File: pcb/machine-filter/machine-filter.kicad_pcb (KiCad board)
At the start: 4 copper layers, 150 x 107 mm, 0 parts

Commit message: Placement step 1: footprints in the PCB, grouped by function; zone sketch
- Footprints brought into the PCB through Konnect (KiCad 10 IPC) and sorted into
  function groups beside their boards (design/groups.py, stage_groups.py,
  tools/konnect_stage.py), plus 8 optional standoff holes and group labels.
- Main-board zone sketch with area budgets for review (design/zone_sketch.py,
  out/zone-sketch.png).
- WIDTH moved to U1 so each CV quad carries one 1V/OCT channel (d).
- gen_sch.py: stable sheet/symbol UUIDs, so rebuilds keep PCB links.
- Both boards 2-layer (d); Konnect setup notes; CLAUDE.md: pin map follows
  the layout.

Co-Authored-By: Claude Opus 5.5 <noreply@anthropic.com>
Claude-Session: https://claude.ai/code/session_01Cf5qNBi3oNHhbCjPHvswth
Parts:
- added A1: Daisy Seed3, filter-module:Daisy_Seed_ES_Sockets, F.Cu at (263.9, 69.5)
- added C1: 10u 25V, filter-module:C_0805, F.Cu at (328.6, 119.7)
- added C10: 1n, filter-module:C_0603, F.Cu at (292.0, 138.7)
- added C100: 100n, filter-module:C_0603, F.Cu at (324.8, 168.2)
- added C11: 1n, filter-module:C_0603, F.Cu at (292.0, 164.2)
- added C12: 1n, filter-module:C_0603, F.Cu at (278.3, 149.6)
- added C13: 1n, filter-module:C_0603, F.Cu at (264.0, 152.6)
- added C14: 1n, filter-module:C_0603, F.Cu at (283.0, 152.6)
- added C15: 1n, filter-module:C_0603, F.Cu at (278.3, 175.1)
- added C16: 1n, filter-module:C_0603, F.Cu at (264.0, 178.1)
- added C17: 1n, filter-module:C_0603, F.Cu at (283.0, 178.1)
- added C2: 100u 35V, Capacitor_SMD:CP_Elec_6.3x7.7, F.Cu at (309.1, 145.2)
- added C20: 100n, filter-module:C_0603, F.Cu at (273.0, 164.2)
- added C21: 100n, filter-module:C_0603, F.Cu at (273.0, 138.7)
- added C3: 10u 25V, filter-module:C_0805, F.Cu at (328.1, 142.6)
- added C4: 100u 35V, Capacitor_SMD:CP_Elec_6.3x7.7, F.Cu at (309.1, 153.9)
- added C5: 100u 35V, Capacitor_SMD:CP_Elec_6.3x7.7, F.Cu at (273.2, 124.4)
- added C50: 330p, filter-module:C_0603, F.Cu at (334.1, 68.8)
- added C52: 330p, filter-module:C_0603, F.Cu at (320.3, 75.8)
- added C6: 100u 35V, Capacitor_SMD:CP_Elec_6.3x7.7, F.Cu at (291.7, 71.6)
- added C60: 47p, filter-module:C_0603, F.Cu at (334.1, 87.4)
- added C62: 47p, filter-module:C_0603, F.Cu at (320.3, 94.4)
- added C7: 100n, filter-module:C_0603, F.Cu at (311.0, 106.0)
- added C70: 100n, filter-module:C_0603, F.Cu at (315.1, 68.8)
- added C71: 100n, filter-module:C_0603, F.Cu at (319.8, 68.8)
- added C72: 100n, filter-module:C_0603, F.Cu at (315.1, 87.4)
- added C73: 100n, filter-module:C_0603, F.Cu at (319.8, 87.4)
- added C80: 100n, Capacitor_THT:C_Disc_D3.0mm_W1.6mm_P2.50mm, F.Cu at (84.8, 65.8)
- added C81: 100n, Capacitor_THT:C_Disc_D3.0mm_W1.6mm_P2.50mm, F.Cu at (65.8, 86.4)
- added C82: 100n, Capacitor_THT:C_Disc_D3.0mm_W1.6mm_P2.50mm, F.Cu at (72.0, 86.4)
- added C83: 100n, Capacitor_THT:C_Disc_D3.0mm_W1.6mm_P2.50mm, F.Cu at (65.8, 116.7)
- added C84: 100n, Capacitor_THT:C_Disc_D3.0mm_W1.6mm_P2.50mm, F.Cu at (72.0, 116.7)
- added D1: red 3 mm, filter-module:LED_3mm_C1A2, F.Cu at (2.94, 93.3)
- added D10: B5819W, filter-module:D_SOD-123, F.Cu at (323.1, 119.6)
- added D11: B5819W, filter-module:D_SOD-123, F.Cu at (322.6, 142.5)
- added D2: red/green 3 mm, filter-module:LED_3mm_Raised, F.Cu at (8.99, 92.1)
- added D3: red/green 3 mm, filter-module:LED_3mm_Raised, F.Cu at (14.8, 92.1)
- added D4: red/green 3 mm, filter-module:LED_3mm_Raised, F.Cu at (20.7, 92.1)
- added D5: red/green 3 mm, filter-module:LED_3mm_Raised, F.Cu at (-42.0, 103.0)
- added D6: red/green 3 mm, filter-module:LED_3mm_Raised, F.Cu at (-36.2, 103.0)
- added D7: red/green 3 mm, filter-module:LED_3mm_Raised, F.Cu at (-30.3, 103.0)
- added D8: red/green 3 mm, filter-module:LED_3mm_Raised, F.Cu at (-24.5, 103.0)
- added D9: red/green 3 mm, filter-module:LED_3mm_Raised, F.Cu at (-18.6, 103.0)
- added FB1: 600R@100MHz 0.5A, filter-module:R_0805_2012Metric, F.Cu at (317.5, 119.7)
- added FB2: 600R@100MHz 0.5A, filter-module:R_0805_2012Metric, F.Cu at (317.0, 142.6)
- added H1: MountingHole_3.2mm_M3, MountingHole:MountingHole_3.2mm_M3, F.Cu at (266.4, 194.8)
- added H11: MountingHole_3.2mm_M3, MountingHole:MountingHole_3.2mm_M3, F.Cu at (-40.2, 156.8)
- added H12: MountingHole_3.2mm_M3, MountingHole:MountingHole_3.2mm_M3, F.Cu at (-32.2, 156.8)
- added H13: MountingHole_3.2mm_M3, MountingHole:MountingHole_3.2mm_M3, F.Cu at (-24.2, 156.8)
- added H14: MountingHole_3.2mm_M3, MountingHole:MountingHole_3.2mm_M3, F.Cu at (-16.2, 156.8)
- added H2: MountingHole_3.2mm_M3, MountingHole:MountingHole_3.2mm_M3, F.Cu at (274.4, 194.8)
- added H3: MountingHole_3.2mm_M3, MountingHole:MountingHole_3.2mm_M3, F.Cu at (282.4, 194.8)
- added H4: MountingHole_3.2mm_M3, MountingHole:MountingHole_3.2mm_M3, F.Cu at (290.4, 194.8)
- added J1: PJ398SM, filter-module:PJ398SM_Jack_ES, F.Cu at (-39.4, 71.0)
- added J10: PJ398SM, filter-module:PJ398SM_Jack_4ms_BentGND, F.Cu at (-37.7, 95.7)
- added J11: PJ398SM, filter-module:PJ398SM_Jack_4ms_BentGND, F.Cu at (-22.8, 95.7)
- added J12: PJ398SM, filter-module:PJ398SM_Jack_4ms_BentGND, F.Cu at (-7.89, 95.7)
- added J13: EURO PWR 2x5, filter-module:Pins_2x05_2.54mm_TH_EurorackPower_Shrouded, F.Cu at (309.4, 129.5)
- added J14: EXPANSION 2x4, filter-module:Pins_2x04_2.54mm_TH, F.Cu at (346.6, 73.2)
- added J15: TF-01A, filter-module:TF-01A, F.Cu at (313.1, 175.3)
- added J2: PJ398SM, filter-module:PJ398SM_Jack_ES, F.Cu at (-28.4, 71.0)
- added J3: PJ398SM, filter-module:PJ398SM_Jack_ES, F.Cu at (-17.3, 71.0)
- added J4: PJ398SM, filter-module:PJ398SM_Jack_ES, F.Cu at (-6.26, 71.0)
- added J5: PJ398SM, filter-module:PJ398SM_Jack_4ms_BentGND, F.Cu at (6.47, 69.5)
- added J6: PJ398SM, filter-module:PJ398SM_Jack_4ms_BentGND, F.Cu at (-37.7, 84.7)
- added J7: PJ398SM, filter-module:PJ398SM_Jack_4ms_BentGND, F.Cu at (-22.8, 84.7)
- added J8: PJ398SM, filter-module:PJ398SM_Jack_4ms_BentGND, F.Cu at (-7.89, 84.7)
- added J9: PJ398SM, filter-module:PJ398SM_Jack_4ms_BentGND, F.Cu at (7.03, 84.7)
- added JA1: 1x15 socket, Connector_PinSocket_2.54mm:PinSocket_1x15_P2.54mm_Vertical, F.Cu at (35.8, 66.5)
- added JA2: 1x13 socket, Connector_PinSocket_2.54mm:PinSocket_1x13_P2.54mm_Vertical, F.Cu at (40.9, 66.5)
- added JA3: 1x10 socket, Connector_PinSocket_2.54mm:PinSocket_1x10_P2.54mm_Vertical, F.Cu at (46.0, 66.5)
- added JB1: 1x15 header, Connector_PinHeader_2.54mm:PinHeader_1x15_P2.54mm_Vertical, F.Cu at (345.7, 90.1)
- added JB2: 1x13 header, Connector_PinHeader_2.54mm:PinHeader_1x13_P2.54mm_Vertical, F.Cu at (350.8, 90.1)
- added JB3: 1x10 header, Connector_PinHeader_2.54mm:PinHeader_1x10_P2.54mm_Vertical, F.Cu at (355.9, 90.1)
- added R1: 3.3 0.75W, filter-module:R_1206_3216Metric, F.Cu at (281.8, 122.0)
- added R10: 100k 0.1%, filter-module:R_0603, F.Cu at (277.7, 138.7)
- added R100: 47k, filter-module:R_0603, F.Cu at (329.5, 168.2)
- added R101: 47k, filter-module:R_0603, F.Cu at (334.3, 168.2)
- added R102: 47k, filter-module:R_0603, F.Cu at (306.0, 182.1)
- added R103: 47k, filter-module:R_0603, F.Cu at (310.8, 182.1)
- added R104: 47k, filter-module:R_0603, F.Cu at (315.5, 182.1)
- added R11: 20k 0.1%, filter-module:R_0603, F.Cu at (287.2, 138.7)
- added R12: 120k 25ppm, filter-module:R_0603, F.Cu at (264.0, 149.6)
- added R13: 20k 0.1%, filter-module:R_0603, F.Cu at (282.5, 138.7)
- added R14: 100k 0.1%, filter-module:R_0603, F.Cu at (277.7, 164.2)
- added R15: 20k 0.1%, filter-module:R_0603, F.Cu at (287.2, 164.2)
- added R16: 120k 25ppm, filter-module:R_0603, F.Cu at (264.0, 175.1)
- added R17: 20k 0.1%, filter-module:R_0603, F.Cu at (282.5, 164.2)
- added R18: 120k, filter-module:R_0603, F.Cu at (268.8, 149.6)
- added R19: 20k, filter-module:R_0603, F.Cu at (273.5, 149.6)
- added R2: 3.3 0.75W, filter-module:R_1206_3216Metric, F.Cu at (264.7, 122.0)
- added R20: 120k, filter-module:R_0603, F.Cu at (283.0, 149.6)
- added R22: 120k, filter-module:R_0603, F.Cu at (287.8, 149.6)
- added R23: 20k, filter-module:R_0603, F.Cu at (292.5, 149.6)
- added R24: 120k, filter-module:R_0603, F.Cu at (268.8, 152.6)
- added R26: 120k, filter-module:R_0603, F.Cu at (273.5, 152.6)
- added R27: 20k, filter-module:R_0603, F.Cu at (278.3, 152.6)
- added R28: 120k, filter-module:R_0603, F.Cu at (287.8, 152.6)
- added R3: 1k, filter-module:R_0603, F.Cu at (315.7, 106.0)
- added R30: 120k, filter-module:R_0603, F.Cu at (268.8, 175.1)
- added R31: 20k, filter-module:R_0603, F.Cu at (273.5, 175.1)
- added R32: 120k, filter-module:R_0603, F.Cu at (283.0, 175.1)
- added R34: 120k, filter-module:R_0603, F.Cu at (287.8, 175.1)
- added R35: 20k, filter-module:R_0603, F.Cu at (292.5, 175.1)
- added R36: 120k, filter-module:R_0603, F.Cu at (268.8, 178.1)
- added R38: 120k, filter-module:R_0603, F.Cu at (273.5, 178.1)
- added R39: 20k, filter-module:R_0603, F.Cu at (278.3, 178.1)
- added R40: 120k, filter-module:R_0603, F.Cu at (287.8, 178.1)
- added R50: 100k, filter-module:R_0603, F.Cu at (324.6, 68.8)
- added R51: 10k, filter-module:R_0603, F.Cu at (329.3, 68.8)
- added R52: 100, filter-module:R_0603, F.Cu at (306.0, 75.8)
- added R54: 100k, filter-module:R_0603, F.Cu at (310.8, 75.8)
- added R55: 10k, filter-module:R_0603, F.Cu at (315.5, 75.8)
- added R56: 100, filter-module:R_0603, F.Cu at (325.0, 75.8)
- added R60: 10k, filter-module:R_0603, F.Cu at (324.6, 87.4)
- added R61: 51k, filter-module:R_0603, F.Cu at (329.3, 87.4)
- added R62: 100, filter-module:R_0603, F.Cu at (306.0, 94.4)
- added R64: 10k, filter-module:R_0603, F.Cu at (310.8, 94.4)
- added R65: 51k, filter-module:R_0603, F.Cu at (315.5, 94.4)
- added R66: 100, filter-module:R_0603, F.Cu at (325.0, 94.4)
- added R70: 1k, filter-module:R_0603, F.Cu at (283.8, 68.8)
- added R71: 1.5k, Resistor_THT:R_Axial_DIN0204_L3.6mm_D1.6mm_P5.08mm_Horizontal, F.Cu at (78.0, 86.4)
- added R72: 1.5k, Resistor_THT:R_Axial_DIN0204_L3.6mm_D1.6mm_P5.08mm_Horizontal, F.Cu at (56.8, 97.2)
- added R73: 1.5k, Resistor_THT:R_Axial_DIN0204_L3.6mm_D1.6mm_P5.08mm_Horizontal, F.Cu at (65.3, 97.2)
- added R74: 1.5k, Resistor_THT:R_Axial_DIN0204_L3.6mm_D1.6mm_P5.08mm_Horizontal, F.Cu at (73.8, 97.2)
- added R75: 1.5k, Resistor_THT:R_Axial_DIN0204_L3.6mm_D1.6mm_P5.08mm_Horizontal, F.Cu at (78.0, 116.7)
- added R76: 1.5k, Resistor_THT:R_Axial_DIN0204_L3.6mm_D1.6mm_P5.08mm_Horizontal, F.Cu at (56.8, 127.5)
- added R77: 1.5k, Resistor_THT:R_Axial_DIN0204_L3.6mm_D1.6mm_P5.08mm_Horizontal, F.Cu at (65.3, 127.5)
- added R78: 1.5k, Resistor_THT:R_Axial_DIN0204_L3.6mm_D1.6mm_P5.08mm_Horizontal, F.Cu at (73.8, 127.5)
- added R80: 10k, Resistor_THT:R_Axial_DIN0204_L3.6mm_D1.6mm_P5.08mm_Horizontal, F.Cu at (82.3, 97.2)
- added R81: 10k, Resistor_THT:R_Axial_DIN0204_L3.6mm_D1.6mm_P5.08mm_Horizontal, F.Cu at (56.8, 100.9)
- added R82: 10k, Resistor_THT:R_Axial_DIN0204_L3.6mm_D1.6mm_P5.08mm_Horizontal, F.Cu at (65.3, 100.9)
- added R83: 10k, Resistor_THT:R_Axial_DIN0204_L3.6mm_D1.6mm_P5.08mm_Horizontal, F.Cu at (73.8, 100.9)
- added R84: 10k, Resistor_THT:R_Axial_DIN0204_L3.6mm_D1.6mm_P5.08mm_Horizontal, F.Cu at (82.3, 127.5)
- added R85: 10k, Resistor_THT:R_Axial_DIN0204_L3.6mm_D1.6mm_P5.08mm_Horizontal, F.Cu at (56.8, 131.2)
- added R86: 10k, Resistor_THT:R_Axial_DIN0204_L3.6mm_D1.6mm_P5.08mm_Horizontal, F.Cu at (65.3, 131.2)
- added R87: 10k, Resistor_THT:R_Axial_DIN0204_L3.6mm_D1.6mm_P5.08mm_Horizontal, F.Cu at (73.8, 131.2)
- added R90: 1M, Resistor_THT:R_Axial_DIN0204_L3.6mm_D1.6mm_P5.08mm_Horizontal, F.Cu at (82.3, 100.9)
- added R91: 1M, Resistor_THT:R_Axial_DIN0204_L3.6mm_D1.6mm_P5.08mm_Horizontal, F.Cu at (56.8, 104.5)
- added R92: 1M, Resistor_THT:R_Axial_DIN0204_L3.6mm_D1.6mm_P5.08mm_Horizontal, F.Cu at (65.3, 104.5)
- added R93: 1M, Resistor_THT:R_Axial_DIN0204_L3.6mm_D1.6mm_P5.08mm_Horizontal, F.Cu at (73.8, 104.5)
- added R94: 1M, Resistor_THT:R_Axial_DIN0204_L3.6mm_D1.6mm_P5.08mm_Horizontal, F.Cu at (82.3, 131.2)
- added R95: 1M, Resistor_THT:R_Axial_DIN0204_L3.6mm_D1.6mm_P5.08mm_Horizontal, F.Cu at (56.8, 134.8)
- added R96: 1M, Resistor_THT:R_Axial_DIN0204_L3.6mm_D1.6mm_P5.08mm_Horizontal, F.Cu at (65.3, 134.8)
- added R97: 1M, Resistor_THT:R_Axial_DIN0204_L3.6mm_D1.6mm_P5.08mm_Horizontal, F.Cu at (73.8, 134.8)
- added RV1: B10k, filter-module:Pot_9mm_SnapIn_ES, F.Cu at (-8.62, 107.1)
- added RV2: B10k, filter-module:Pot_9mm_SnapIn_ES, F.Cu at (5.54, 107.1)
- added RV3: B10k, filter-module:Pot_9mm_SnapIn_ES, F.Cu at (19.7, 107.1)
- added RV4: B10k, filter-module:Pot_9mm_SnapIn_ES, F.Cu at (-37.9, 121.9)
- added RV5: B10k, filter-module:Pot_9mm_SnapIn_ES, F.Cu at (-23.7, 121.9)
- added RV6: B10k, filter-module:Pot_9mm_SnapIn_ES, F.Cu at (-9.56, 121.9)
- added RV7: B10k, filter-module:Pot_9mm_SnapIn_ES, F.Cu at (4.58, 121.9)
- added RV8: B10k, filter-module:Pot_9mm_SnapIn_ES, F.Cu at (18.7, 121.9)
- added RV9: B10k, filter-module:Pot_9mm_SnapIn_ES, F.Cu at (-37.9, 136.7)
- added U1: LMV324, filter-module:SOIC-14_3.9x8.65mm_Pitch1.27mm, F.Cu at (266.1, 168.1)
- added U2: LMV324, filter-module:SOIC-14_3.9x8.65mm_Pitch1.27mm, F.Cu at (266.1, 142.6)
- added U3: TL072, filter-module:SOIC-8_3.9x4.9mm_Pitch1.27mm, F.Cu at (308.2, 70.8)
- added U4: TL072, filter-module:SOIC-8_3.9x4.9mm_Pitch1.27mm, F.Cu at (308.2, 89.4)
- added U5: LM4040-10, filter-module:SOT-23, F.Cu at (306.1, 107.0)
- added U6: 74HC4051, filter-module:SOIC-16_3.9x9.9mm_Pitch1.27mm, F.Cu at (78.5, 70.0)
- added U7: LM324, filter-module:SOIC-14_3.9x8.65mm_Pitch1.27mm, F.Cu at (59.5, 90.0)
- added U8: LM324, filter-module:SOIC-14_3.9x8.65mm_Pitch1.27mm, F.Cu at (59.5, 120.3)
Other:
- board text added: "1 SEED3 (+ supply filter)"
- board text added: "2 CV U1: WIDTH (1V/OCT), EQ GAIN, DIST, SMPL RATE"
- board text added: "2 CV U2: BASE (1V/OCT), HP RES, LP RES, EQ FREQ"
- board text added: "3 AUDIO IN U3"
- board text added: "3 AUDIO OUT U4"
- board text added: "4 -10V REF U5"
- board text added: "5 POWER ENTRY J13"
- board text added: "6 EXPANSION J14"
- board text added: "6 microSD J15 (optional)"
- board text added: "7 HEADERS"
- board text added: "8 STANDOFFS (optional)"
- board text added: "LED DRIVERS U7"
- board text added: "LED DRIVERS U8"
- board text added: "PANEL PARTS (fixed by the panel)"
- board text added: "POT MUX U6"

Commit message: Placement step 2: Seed3 placed with its group; VIN trace; board set to 2 layers
- A1 on the main board's back at its USB-rule spot (pins checked against the
  zone sketch), supply filter R1-C5-R2-C6 at VIN, R70 at pin 12, and the first
  trace: Seed3 pin 39 -> C6 (0.5 mm, B.Cu).
- design/placement.py records each step; tools/konnect_place.py applies it
  through Konnect, checks pad positions before routing, and saves.
- Copper layers 4 -> 2 (d), set in KiCad's Board Setup.

Co-Authored-By: Claude Opus 5.5 <noreply@anthropic.com>
Claude-Session: https://claude.ai/code/session_01Cf5qNBi3oNHhbCjPHvswth
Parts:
- A1, C5, C6, R1, R2, R70: moved to B.Cu
- moved C6 88.1 mm to (237.5, 141.0)
- moved R70 86.6 mm to (208.5, 111.5), turned to 90 degrees
- moved A1 86.2 mm to (213.6, 139.5)
- moved R1 52.2 mm to (244.5, 158.5)
- moved C5 45.5 mm to (237.5, 152.5)
- moved R2 37.0 mm to (237.5, 147.0)
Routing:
- net VIN: track 0.00 -> 10.00 mm
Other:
- copper layers 4 -> 2

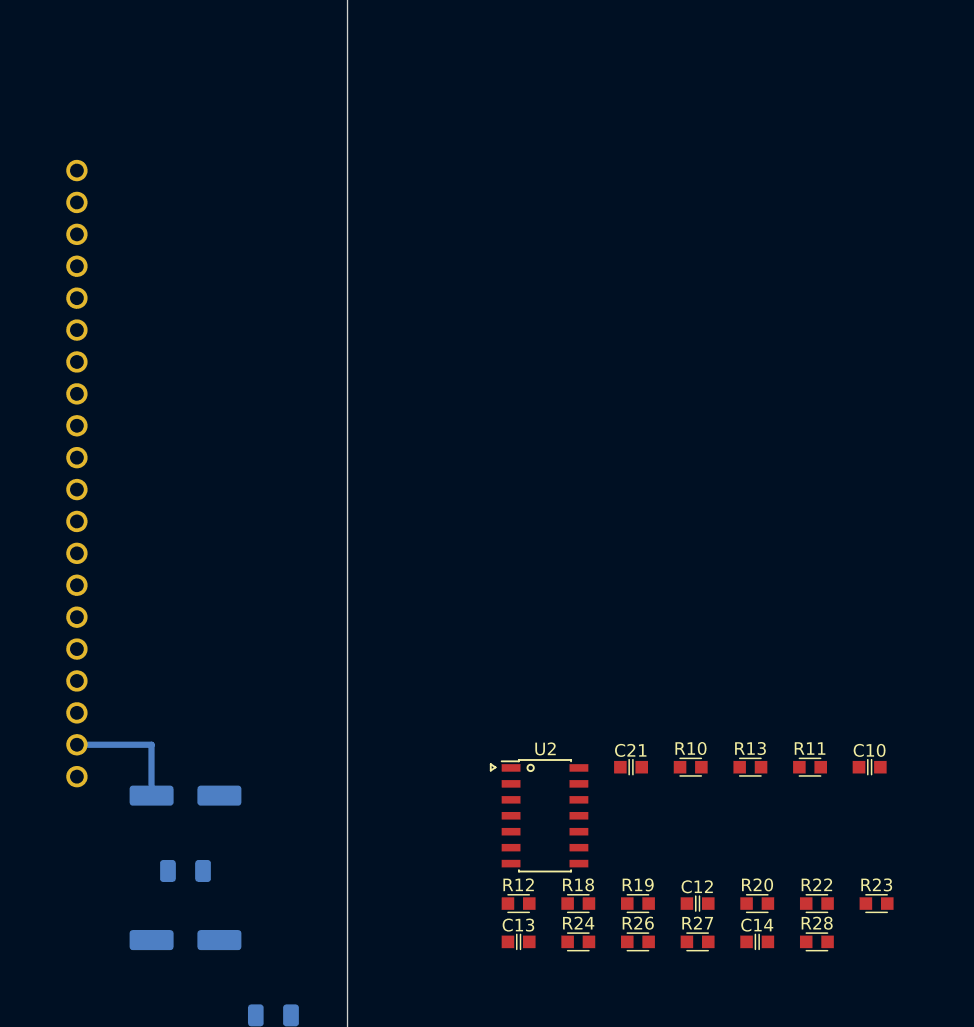
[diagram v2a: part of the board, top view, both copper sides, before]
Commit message: Placement step 3: U2 and its CV group; trace U2 pin 1 (BASE) -> Seed3 pin 23
Co-Authored-By: Claude Opus 5.5 <noreply@anthropic.com>
Claude-Session: https://claude.ai/code/session_01Cf5qNBi3oNHhbCjPHvswth
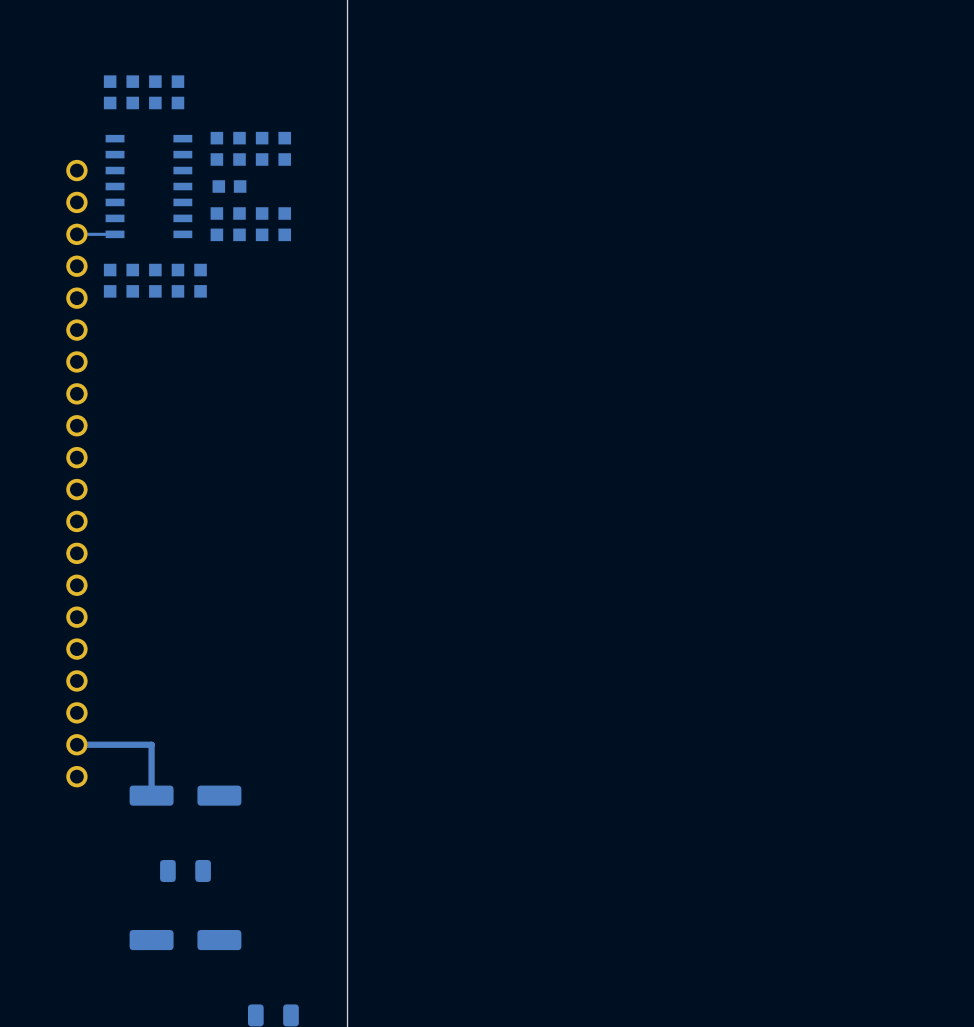
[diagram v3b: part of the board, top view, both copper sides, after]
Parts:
- C10, C12, C13, C14, C21, R10, R11, R12, R13, R18, R19, R20, R22, R23, R24, R26, R27, R28, U2: moved to B.Cu
- moved R20 79.4 mm to (236.9, 85.0), turned to -90 degrees
- moved R23 78.6 mm to (241.8, 89.5), turned to -90 degrees
- moved C12 77.7 mm to (235.1, 85.0), turned to -90 degrees
- moved R22 76.8 mm to (240.0, 89.5), turned to -90 degrees
- moved R19 76.1 mm to (233.3, 85.0), turned to -90 degrees
- moved R18 74.6 mm to (231.5, 85.0), turned to -90 degrees
- moved R28 71.1 mm to (245.4, 95.5), turned to -90 degrees
- moved C14 69.4 mm to (243.6, 95.5), turned to -90 degrees
- moved R27 67.8 mm to (241.8, 95.5), turned to -90 degrees
- moved R24 67.3 mm to (245.4, 89.5), turned to -90 degrees
- moved C10 67.3 mm to (236.9, 100.0), turned to -90 degrees
- moved C13 66.4 mm to (243.6, 89.5), turned to -90 degrees
- moved R26 66.3 mm to (240.0, 95.5), turned to -90 degrees
- moved R11 64.9 mm to (235.1, 100.0), turned to -90 degrees
- moved R13 62.6 mm to (233.3, 100.0), turned to -90 degrees
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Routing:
- net ADC_BASE: track 0.00 -> 3.04 mm

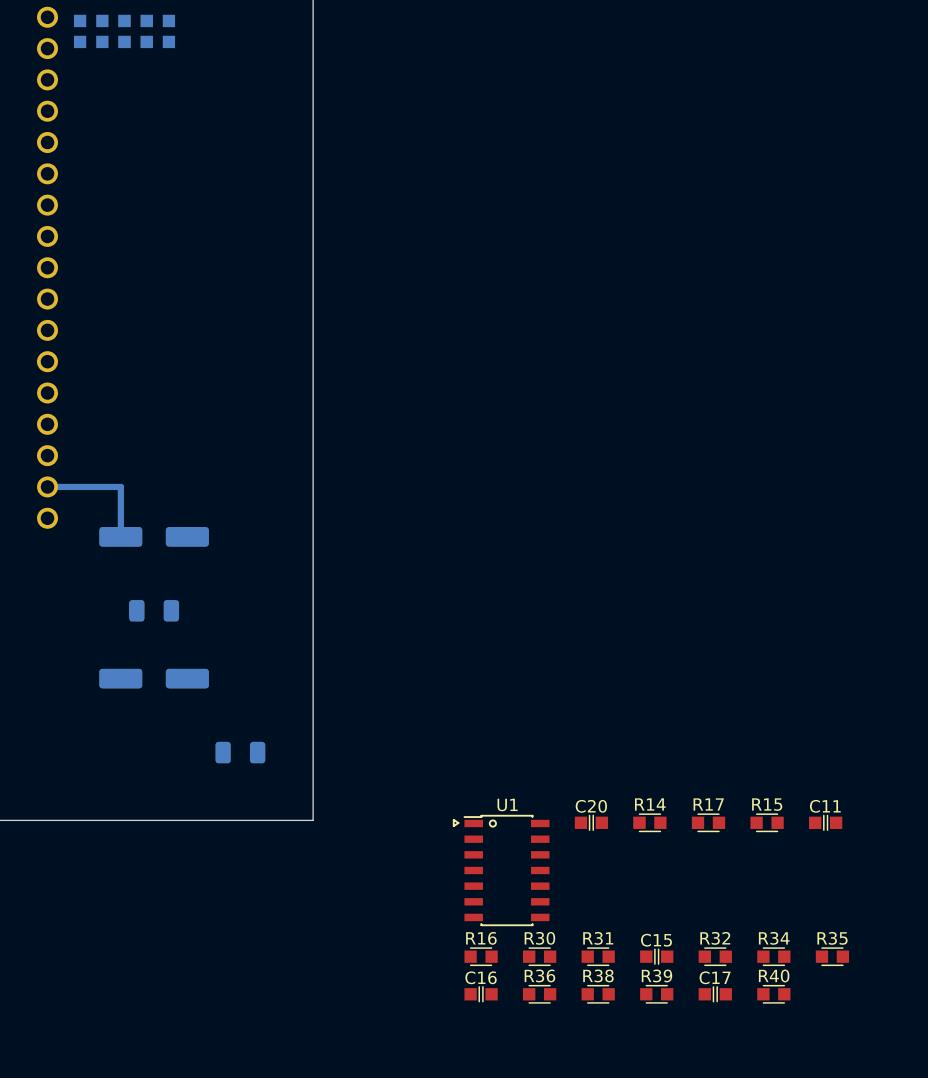
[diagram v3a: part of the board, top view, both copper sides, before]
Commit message: Placement step 4: U1 and its CV group; ADC pins re-matched to the placed chips
Re-match pending d's OK (d questioned doing it now): tools/rematch_adc.py,
pinmap ADC_UNIT/SEED_ADC, schematic rebuilt, firmware and placement docs
updated, PCB pads reassigned (U1 re-added: its unit A moved sheets).
WIDTH trace not drawn yet.

Co-Authored-By: Claude Opus 5.5 <noreply@anthropic.com>
Claude-Session: https://claude.ai/code/session_01Cf5qNBi3oNHhbCjPHvswth
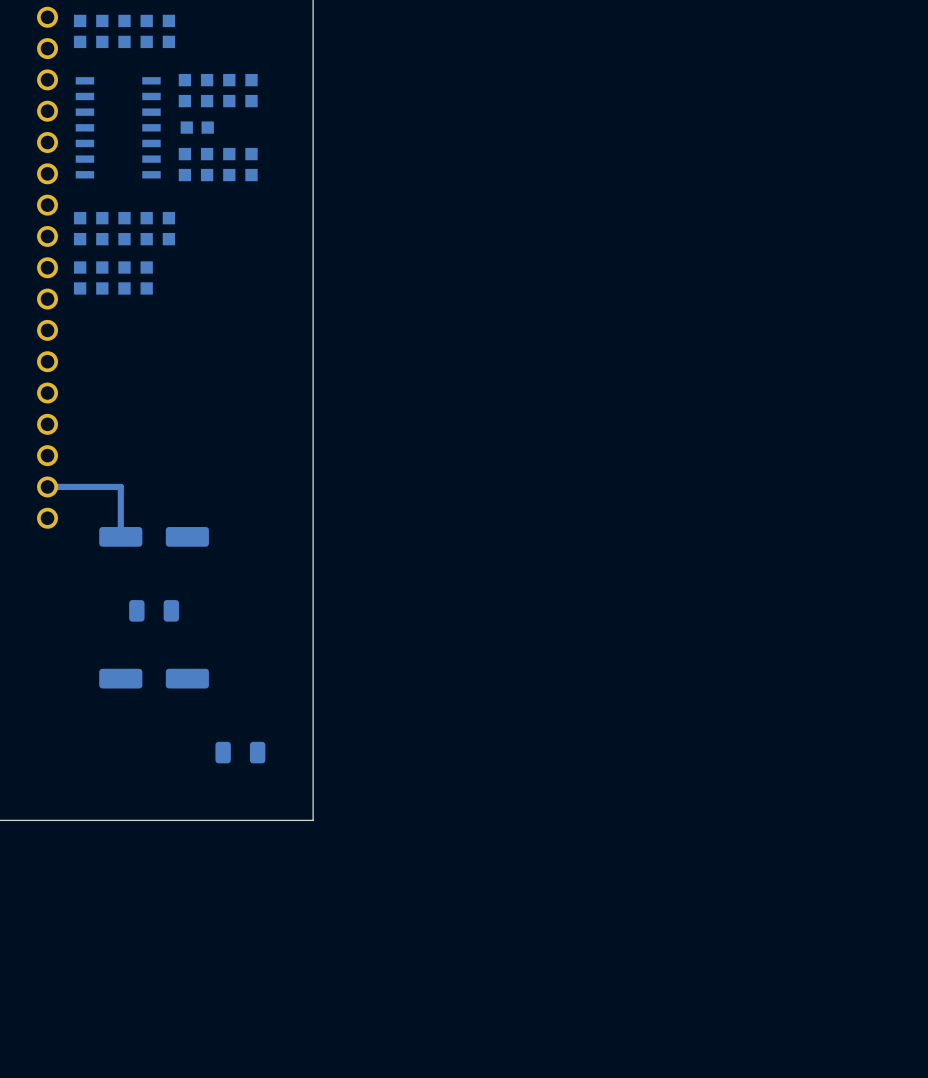
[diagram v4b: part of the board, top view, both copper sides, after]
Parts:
- C11, C15, C16, C17, C20, R14, R15, R16, R17, R30, R31, R32, R34, R35, R36, R38, R39, R40, U1: moved to B.Cu
- moved R35 86.7 mm to (241.8, 104.8), turned to 90 degrees
- moved R34 85.0 mm to (240.0, 104.8), turned to 90 degrees
- moved R40 79.5 mm to (245.4, 110.8), turned to 90 degrees
- moved C17 78.0 mm to (243.6, 110.8), turned to 90 degrees
- moved R36 76.9 mm to (245.4, 104.8), turned to 90 degrees
- moved R39 76.6 mm to (241.8, 110.8), turned to 90 degrees
- moved C16 76.1 mm to (243.6, 104.8), turned to 90 degrees
- moved R38 75.2 mm to (240.0, 110.8), turned to 90 degrees
- moved C11 73.2 mm to (236.9, 116.0), turned to 90 degrees
- moved R32 71.8 mm to (236.9, 120.0), turned to 90 degrees
- moved R15 71.0 mm to (235.1, 116.0), turned to 90 degrees
- moved C15 70.0 mm to (235.1, 120.0), turned to 90 degrees
- moved R17 68.9 mm to (233.3, 116.0), turned to 90 degrees
- moved R31 68.2 mm to (233.3, 120.0), turned to 90 degrees
- moved U1 68.0 mm to (234.6, 107.8)
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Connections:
- A1 pad 22: ADC_WIDTH -> ADC_HPRES
- A1 pad 24: POT_VOL -> ADC_LPRES
- A1 pad 25: ADC_LPRES -> ADC_EQF
- A1 pad 26: ADC_HPRES -> ADC_EQG
- A1 pad 27: ADC_EQF -> ADC_DIST
- A1 pad 28: ADC_EQG -> POT_VOL
- A1 pad 29: unconnected-(A1-D22-Pad29) -> ADC_WIDTH
- A1 pad 30: ADC_DIST -> ADC_SRR
- A1 pad 31: ADC_SRR -> POT_MUX
- A1 pad 32: POT_MUX -> unconnected-(A1-D25-Pad32)
- C11 pad 1: Net-(U1D--) -> Net-(U1A--)
- C15 pad 1: Net-(U1A--) -> Net-(U1B--)
- C17 pad 1: Net-(U1B--) -> Net-(U1D--)
- R15 pad 1: Net-(U1D--) -> Net-(U1A--)
- R16 pad 1: Net-(U1D--) -> Net-(U1A--)
- R17 pad 2: Net-(U1D--) -> Net-(U1A--)
- R30 pad 2: Net-(U1A--) -> Net-(U1B--)
- R31 pad 1: Net-(U1A--) -> Net-(U1B--)
- R32 pad 1: Net-(U1A--) -> Net-(U1B--)
- R38 pad 2: Net-(U1B--) -> Net-(U1D--)
- R39 pad 1: Net-(U1B--) -> Net-(U1D--)
- R40 pad 1: Net-(U1B--) -> Net-(U1D--)
- U1 pad 1: ADC_EQG -> ADC_WIDTH
- U1 pad 14: ADC_WIDTH -> ADC_SRR
- U1 pad 7: ADC_SRR -> ADC_EQG

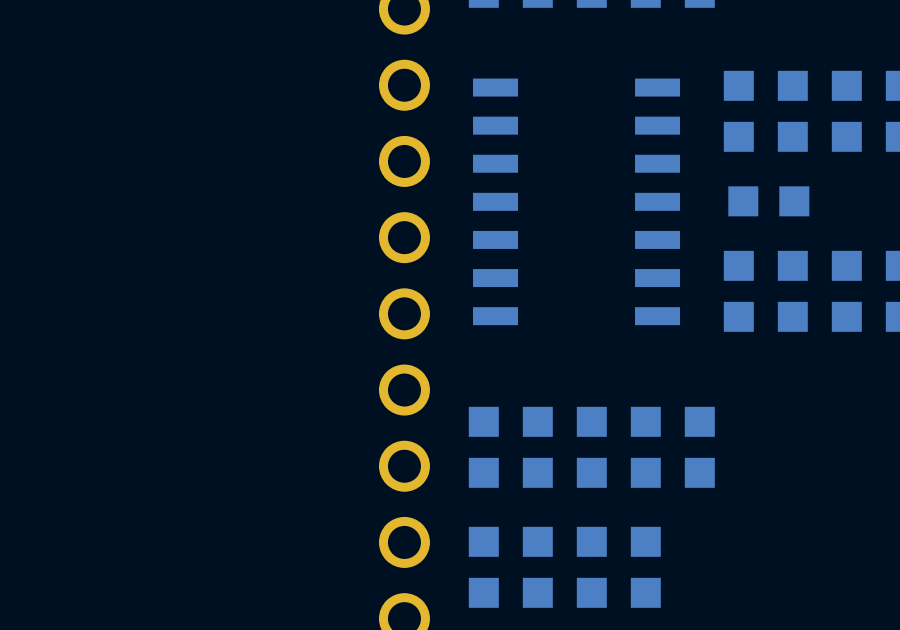
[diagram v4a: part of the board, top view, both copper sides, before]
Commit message: Placement step 4: WIDTH trace U1 pin 1 -> Seed3 pin 29; workflow notes
Co-Authored-By: Claude Opus 5.5 <noreply@anthropic.com>
Claude-Session: https://claude.ai/code/session_01Cf5qNBi3oNHhbCjPHvswth
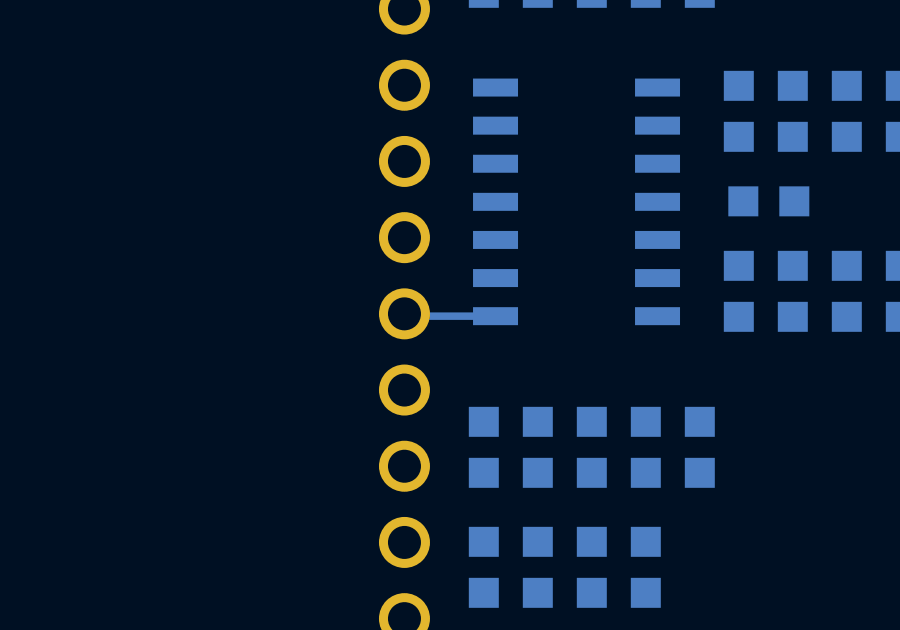
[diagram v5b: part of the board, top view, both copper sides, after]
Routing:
- net ADC_WIDTH: track 0.00 -> 3.11 mm
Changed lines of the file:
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@@
+	)
+	(segment
+		(start 231.89 111.627)
+		(end 228.855 111.627)
+		(width 0.25)
+		(layer "B.Cu")
+		(net "ADC_WIDTH")
+	)
+	(segment
+		(start 228.855 111.627)
+		(end 228.855 111.55)
+		(width 0.25)
+		(layer "B.Cu")
+		(net "ADC_WIDTH")
 	)
 	(segment
